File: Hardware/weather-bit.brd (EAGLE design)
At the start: 68.6 x 58.4 mm, 47 parts, among them J2 RJ11, J3 RJ11, J6 455-1750-1-ND, J7 455-1750-1-ND, J8 Qwiic (vertical), J9 1X04_SMD_STRAIGHT_COMBO, U1 BME280, U2 micro:bit

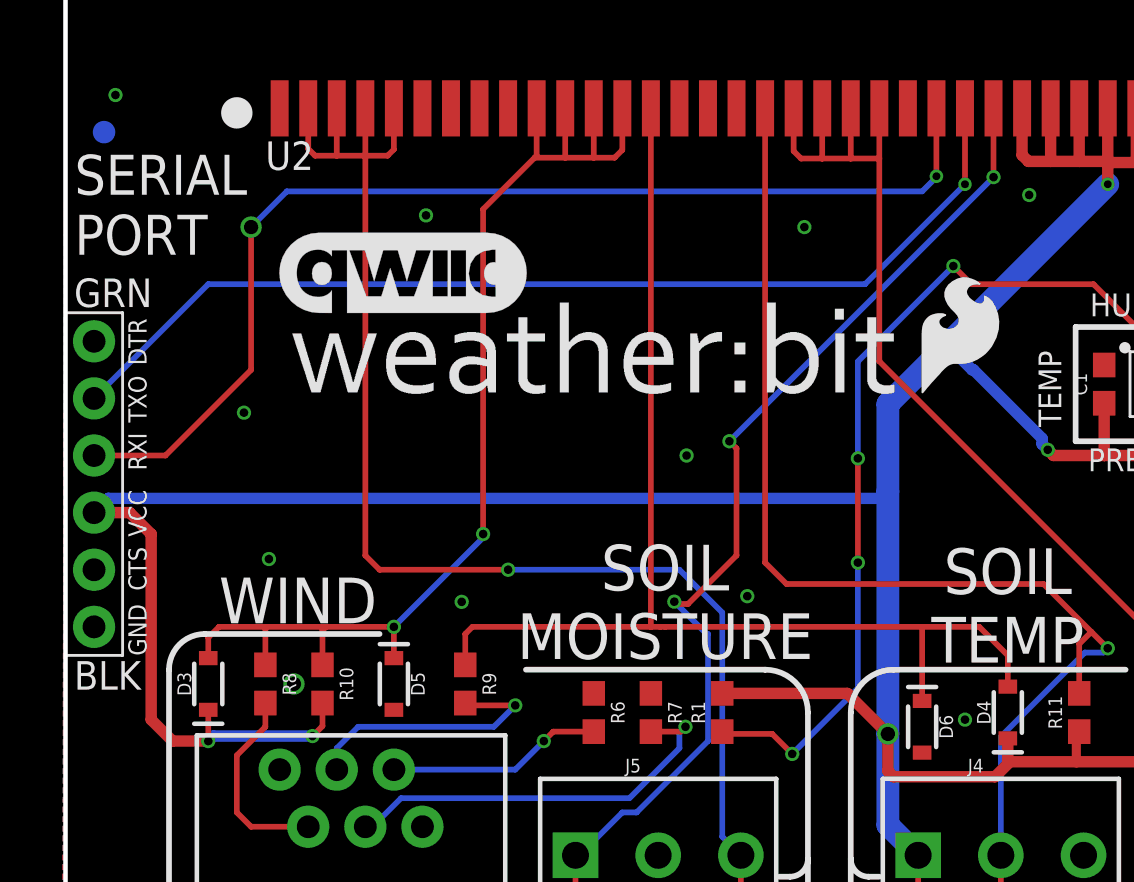
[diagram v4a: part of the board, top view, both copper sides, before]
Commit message: Moved to SMT vertical female header for Serial port
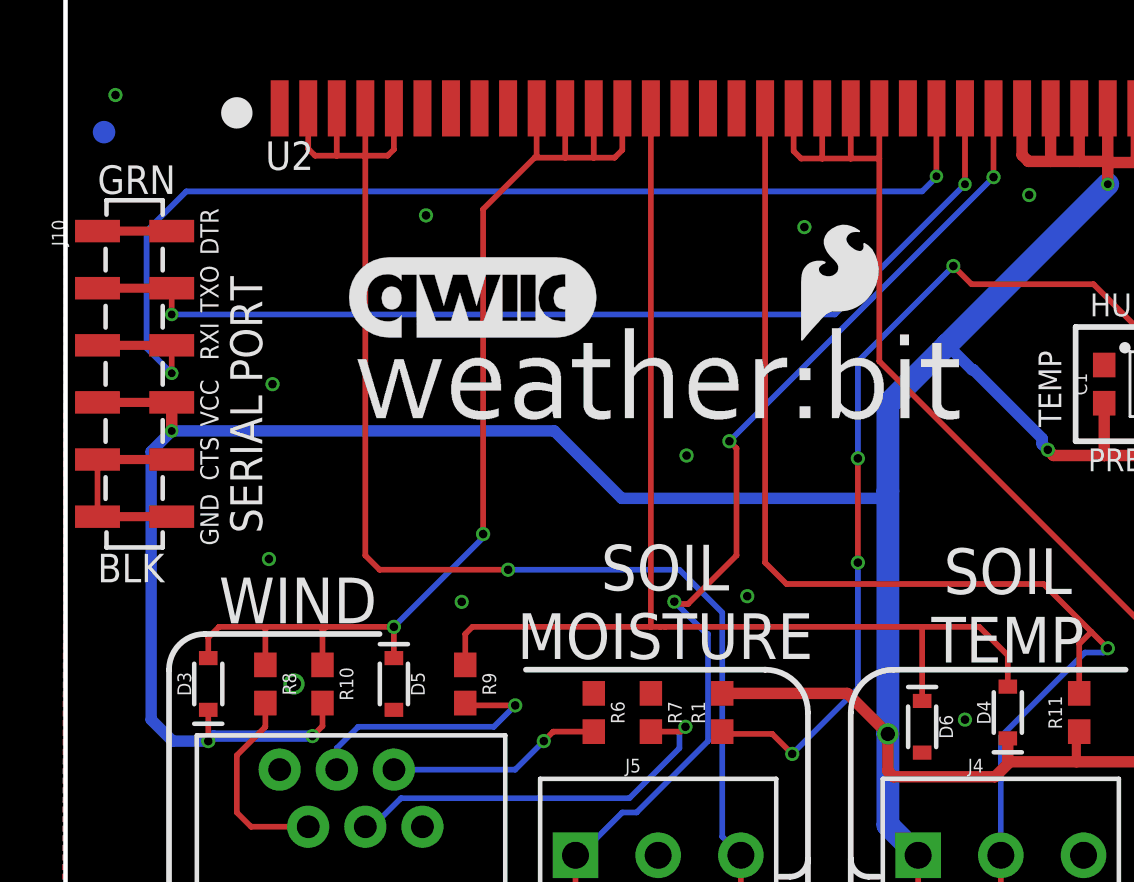
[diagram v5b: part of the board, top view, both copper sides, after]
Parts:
- removed J1: (no value), SparkFun-Connectors:6_PIN_SERIAL_TARGET_SIDE_W_SILK
- added J10: (no value), SparkFun-Connectors:6_PIN_SERIAL_TARGET_SIDE_VERT_SMT
- moved U$1 5.85 mm to (32.4, 35.3)
- moved U$6 3.29 mm to (18.1, 37.5)
- moved U$2 3.11 mm to (12.8, 31.9)
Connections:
- net 3.3V: now also J10.4, J10.4-2; no longer J1.P$4
- net GND: now also J10.5, J10.5-2, J10.6, J10.6-2; no longer J1.P$5, J1.P$6
- net RXI: now also J10.3, J10.3-2; no longer J1.P$3
- net TXO: now also J10.2, J10.2-2; no longer J1.P$2
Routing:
- net GND: track 0.00 -> 5.84 mm
- net 3.3V: track 191.9 -> 196.1 mm, vias 5 -> 6
- net RXI: track 49.4 -> 50.5 mm
- net TXO: track 46.1 -> 45.5 mm, vias 1 -> 2
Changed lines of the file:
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@@
 <text x="60.491371875" y="31.6103" size="0.8128" layer="21" font="vector" ratio="15" rot="SR0">SDA</text>
 <text x="60.54725" y="29.01441875" size="0.8128" layer="21" font="vector" ratio="15" rot="SR0">SCL</text>
-<text x="0.402765625" y="39.40965" size="1.778" layer="21" font="vector" ratio="15">SERIAL
-PORT</text>
+<text x="8.74875" y="27.021965625" size="1.4224" layer="21" font="vector" ratio="15" rot="R90">SERIAL PORT</text>
 <text x="62.007828125" y="39.382675" size="1.778" layer="21" font="vector" ratio="15">I2C
 PORT</text>
@@
 <attribute name="VALUE" value="1X04_SMD_STRAIGHT_COMBO" x="67.5132" y="28.2194" size="0.6096" layer="27" font="vector" ratio="20" rot="R90"/>
 </element>
-<element name="J1" library="SparkFun-Connectors" package="6_PIN_SERIAL_TARGET_SIDE_W_SILK" value="" x="1.27" y="29.21" smashed="yes" rot="R270"/>
-<element name="U$1" library="SparkFun-Aesthetics" package="SFE_LOGO_FLAME_.2" value="" x="37.762409375" y="33.012659375" smashed="yes"/>
-<element name="U$2" library="Micro_Bit_LOGOS" package="LOGO-WEATHERBIT" value="" x="9.907446875" y="33.02" smashed="yes"/>
+<element name="U$1" library="SparkFun-Aesthetics" package="SFE_LOGO_FLAME_.2" value="" x="32.403009375" y="35.349459375" smashed="yes"/>
+<element name="U$2" library="Micro_Bit_LOGOS" package="LOGO-WEATHERBIT" value="" x="12.803046875" y="31.877" smashed="yes"/>
 <element name="U$3" library="Micro_Bit_LOGOS" package="LOGO-WEATHERBIT" value="" x="42.4434" y="25.222196875" smashed="yes" rot="MR0"/>
 <element name="U$4" library="SparkFun-Aesthetics" package="ORDERING_INSTRUCTIONS" value="" x="1.143" y="-16.637" smashed="yes"/>
@@
 </element>
 <element name="U$5" library="SparkFun-Aesthetics" package="QWIIC_5MM" value="" x="57.4294" y="37.084" smashed="yes"/>
-<element name="U$6" library="SparkFun-Aesthetics" package="QWIIC_11MM" value="" x="15.0368" y="38.5572" smashed="yes"/>
+<element name="U$6" library="SparkFun-Aesthetics" package="QWIIC_11MM" value="" x="18.1356" y="37.465" smashed="yes"/>
 <element name="U$7" library="SparkFun-Aesthetics" package="QWIIC_11MM" value="" x="48.768" y="26.6954" smashed="yes" rot="MR0"/>
 <element name="U2" library="SparkFun-Connectors" package="MICRO:BIT-RA_SMD" value="micro:bit" x="34.29" y="52.07" smashed="yes">
@@
 <attribute name="VALUE" x="53.34" y="43.18" size="1.27" layer="27" font="vector"/>
 </element>
+<element name="J10" library="SparkFun-Connectors" package="6_PIN_SERIAL_TARGET_SIDE_VERT_SMT" value="" x="3.0734" y="40.4622" smashed="yes" rot="R270">
+<attribute name="NAME" x="-0.6096" y="40.9702" size="0.6096" layer="25" font="vector" ratio="20" rot="R270"/>
+<attribute name="VALUE" x="-1.4986" y="40.9702" size="0.6096" layer="27" font="vector" ratio="20" rot="R270"/>
+</element>
 </elements>
 <signals>
@@
 <polygon width="0.254" layer="1" isolate="0.3048">
 <vertex x="0" y="58.42"/>
-<vertex x="-0.13788125" y="-0.3175"/>
 <vertex x="-0.13788125" y="-0.3175"/>
 <vertex x="68.44211875" y="-0.3175"/>
@@
 <via x="65.56375" y="12.54125" extent="1-16" drill="0.381"/>
 <via x="66.04" y="45.4025" extent="1-16" drill="0.381"/>
-<via x="7.9375" y="32.385" extent="1-16" drill="0.381"/>
+<via x="9.2075" y="33.655" extent="1-16" drill="0.381"/>
 <via x="9.04875" y="25.87625" extent="1-16" drill="0.381"/>
 <via x="2.2225" y="46.51375" extent="1-16" drill="0.381"/>
@@
 <via x="10.16" y="20.32" extent="1-16" drill="0.635"/>
 <via x="13.97" y="10.16" extent="1-16" drill="0.381"/>
-<contactref element="J1" pad="P$6"/>
-<contactref element="J1" pad="P$5"/>
 <via x="60.48375" y="40.64" extent="1-16" drill="0.381"/>
 <via x="42.861228125" y="42.067478125" extent="1-16" drill="0.381"/>
@@
 <contactref element="U2" pad="P$35"/>
 <contactref element="U2" pad="P$36"/>
+<contactref element="J10" pad="5-2"/>
+<contactref element="J10" pad="5"/>
+<contactref element="J10" pad="6-2"/>
+<contactref element="J10" pad="6"/>
+<wire x1="4.7234" y1="30.3022" x2="1.4234" y2="30.3022" width="0.254" layer="1"/>
+<wire x1="1.4234" y1="30.3022" x2="1.4234" y2="27.7622" width="0.254" layer="1"/>
 </signal>
 <signal name="3.3V">
@@
 <wire x1="37.9222" y1="5.2578" x2="39.37" y2="3.81" width="0.254" layer="1"/>
 <contactref element="J9" pad="3"/>
-<contactref element="J1" pad="P$4"/>
 <via x="6.35" y="17.78" extent="1-16" drill="0.381"/>
 <via x="10.9855" y="18.00225" extent="1-16" drill="0.381"/>
@@
 <wire x1="36.83" y1="16.1925" x2="41.3385" y2="16.1925" width="0.508" layer="1"/>
 <wire x1="41.3385" y1="16.1925" x2="41.91" y2="16.764" width="0.508" layer="1"/>
-<wire x1="36.2585" y1="28.575" x2="36.576" y2="28.8925" width="0.508" layer="16"/>
-<wire x1="36.2585" y1="28.575" x2="1.905" y2="28.575" width="0.508" layer="16"/>
-<wire x1="1.27" y1="27.94" x2="2.8575" y2="27.94" width="0.508" layer="1"/>
-<wire x1="2.8575" y1="27.94" x2="3.81" y2="26.9875" width="0.508" layer="1"/>
-<wire x1="3.81" y1="26.9875" x2="3.81" y2="18.7325" width="0.508" layer="1"/>
-<wire x1="3.81" y1="18.7325" x2="4.7625" y2="17.78" width="0.508" layer="1"/>
-<wire x1="4.7625" y1="17.78" x2="6.35" y2="17.78" width="0.508" layer="1"/>
+<wire x1="36.576" y1="28.8925" x2="36.2585" y2="28.575" width="0.508" layer="16"/>
+<wire x1="4.7625" y1="17.78" x2="3.81" y2="18.7325" width="0.508" layer="16"/>
+<wire x1="4.7625" y1="17.78" x2="6.35" y2="17.78" width="0.508" layer="16"/>
 <wire x1="42.00525" y1="16.85925" x2="44.958" y2="16.85925" width="0.508" layer="1"/>
 <wire x1="44.958" y1="16.85925" x2="50.51425" y2="16.85925" width="0.508" layer="1"/>
@@
 <wire x1="41.91" y1="17.9" x2="41.91" y2="16.9545" width="0.508" layer="1"/>
 <wire x1="41.91" y1="16.9545" x2="42.00525" y2="16.85925" width="0.508" layer="1"/>
-<wire x1="1.905" y1="28.575" x2="1.27" y2="27.94" width="0.508" layer="16"/>
 <contactref element="R11" pad="1"/>
 <wire x1="43.434" y1="31.242" x2="43.434" y2="30.988" width="0.508" layer="16"/>
@@
 <wire x1="47.76125" y1="32.63" x2="47.76125" y2="30.49615" width="0.254" layer="1"/>
 <wire x1="47.76125" y1="30.49615" x2="47.7774" y2="30.48" width="0.254" layer="1"/>
+<contactref element="J10" pad="4"/>
+<contactref element="J10" pad="4-2"/>
+<wire x1="3.81" y1="30.6578" x2="4.7244" y2="31.5722" width="0.508" layer="16"/>
+<via x="4.7244" y="31.5722" extent="1-16" drill="0.35"/>
+<wire x1="3.81" y1="18.7325" x2="3.81" y2="30.6578" width="0.508" layer="16"/>
+<wire x1="4.7234" y1="32.8422" x2="4.7244" y2="32.8412" width="0.508" layer="1"/>
+<wire x1="4.7244" y1="32.8412" x2="4.7244" y2="31.5722" width="0.508" layer="1"/>
+<wire x1="21.7424" y1="31.5722" x2="4.7244" y2="31.5722" width="0.508" layer="16"/>
+<wire x1="36.2585" y1="28.575" x2="24.7396" y2="28.575" width="0.508" layer="16"/>
+<wire x1="24.7396" y1="28.575" x2="21.7424" y2="31.5722" width="0.508" layer="16"/>
+<wire x1="4.7234" y1="32.8422" x2="1.4234" y2="32.8422" width="0.254" layer="1"/>
 </signal>
 <signal name="N$2">
@@
 </signal>
 <signal name="RXI">
-<wire x1="9.8425" y1="42.2275" x2="38.1" y2="42.2275" width="0.254" layer="16"/>
-<contactref element="J1" pad="P$3"/>
-<via x="8.255" y="40.64" extent="1-16" drill="0.635"/>
-<wire x1="8.255" y1="34.29" x2="4.445" y2="30.48" width="0.254" layer="1"/>
-<wire x1="4.445" y1="30.48" x2="1.27" y2="30.48" width="0.254" layer="1"/>
-<wire x1="9.8425" y1="42.2275" x2="8.255" y2="40.64" width="0.254" layer="16"/>
-<wire x1="8.255" y1="34.29" x2="8.255" y2="40.64" width="0.254" layer="1"/>
 <contactref element="U2" pad="P$24"/>
-<wire x1="38.1" y1="42.2275" x2="38.735" y2="42.8625" width="0.254" layer="16"/>
+<wire x1="38.735" y1="42.8625" x2="38.1" y2="42.2275" width="0.254" layer="16"/>
 <wire x1="38.735" y1="42.8625" x2="38.735" y2="42.9006" width="0.254" layer="16"/>
 <via x="38.735" y="42.9006" extent="1-16" drill="0.35"/>
 <wire x1="38.735" y1="42.9006" x2="38.735" y2="45.92" width="0.254" layer="1"/>
+<contactref element="J10" pad="3-2"/>
+<contactref element="J10" pad="3"/>
+<wire x1="5.3721" y1="42.2275" x2="3.6068" y2="40.4622" width="0.254" layer="16"/>
+<wire x1="3.6068" y1="35.2552" x2="3.6068" y2="40.4622" width="0.254" layer="16"/>
+<wire x1="3.6068" y1="35.2552" x2="4.7244" y2="34.1376" width="0.254" layer="16"/>
+<via x="4.7244" y="34.1376" extent="1-16" drill="0.35"/>
+<wire x1="38.1" y1="42.2275" x2="5.3721" y2="42.2275" width="0.254" layer="16"/>
+<wire x1="4.7234" y1="35.3822" x2="1.4234" y2="35.3822" width="0.254" layer="1"/>
+<wire x1="4.7234" y1="35.3822" x2="4.7244" y2="35.3812" width="0.254" layer="1"/>
+<wire x1="4.7244" y1="35.3812" x2="4.7244" y2="34.1376" width="0.254" layer="1"/>
 </signal>
 <signal name="TXO">
-<wire x1="40.005" y1="42.545" x2="35.56" y2="38.1" width="0.254" layer="16"/>
-<wire x1="35.56" y1="38.1" x2="6.35" y2="38.1" width="0.254" layer="16"/>
-<contactref element="J1" pad="P$2"/>
-<wire x1="6.35" y1="38.1" x2="1.27" y2="33.02" width="0.254" layer="16"/>
 <contactref element="U2" pad="P$25"/>
 <wire x1="40.005" y1="45.92" x2="40.005" y2="42.545" width="0.254" layer="1"/>
 <via x="40.005" y="42.545" extent="1-16" drill="0.35"/>
+<contactref element="J10" pad="2-2"/>
+<contactref element="J10" pad="2"/>
+<wire x1="34.2138" y1="36.7538" x2="4.7244" y2="36.7538" width="0.254" layer="16"/>
+<via x="4.7244" y="36.7538" extent="1-16" drill="0.35"/>
+<wire x1="40.005" y1="42.545" x2="34.2138" y2="36.7538" width="0.254" layer="16"/>
+<wire x1="4.7244" y1="37.9212" x2="4.7244" y2="36.7538" width="0.254" layer="1"/>
+<wire x1="1.4234" y1="37.9222" x2="4.7234" y2="37.9222" width="0.254" layer="1"/>
+<wire x1="4.7234" y1="37.9222" x2="4.7244" y2="37.9212" width="0.254" layer="1"/>
 </signal>
 <signal name="11">

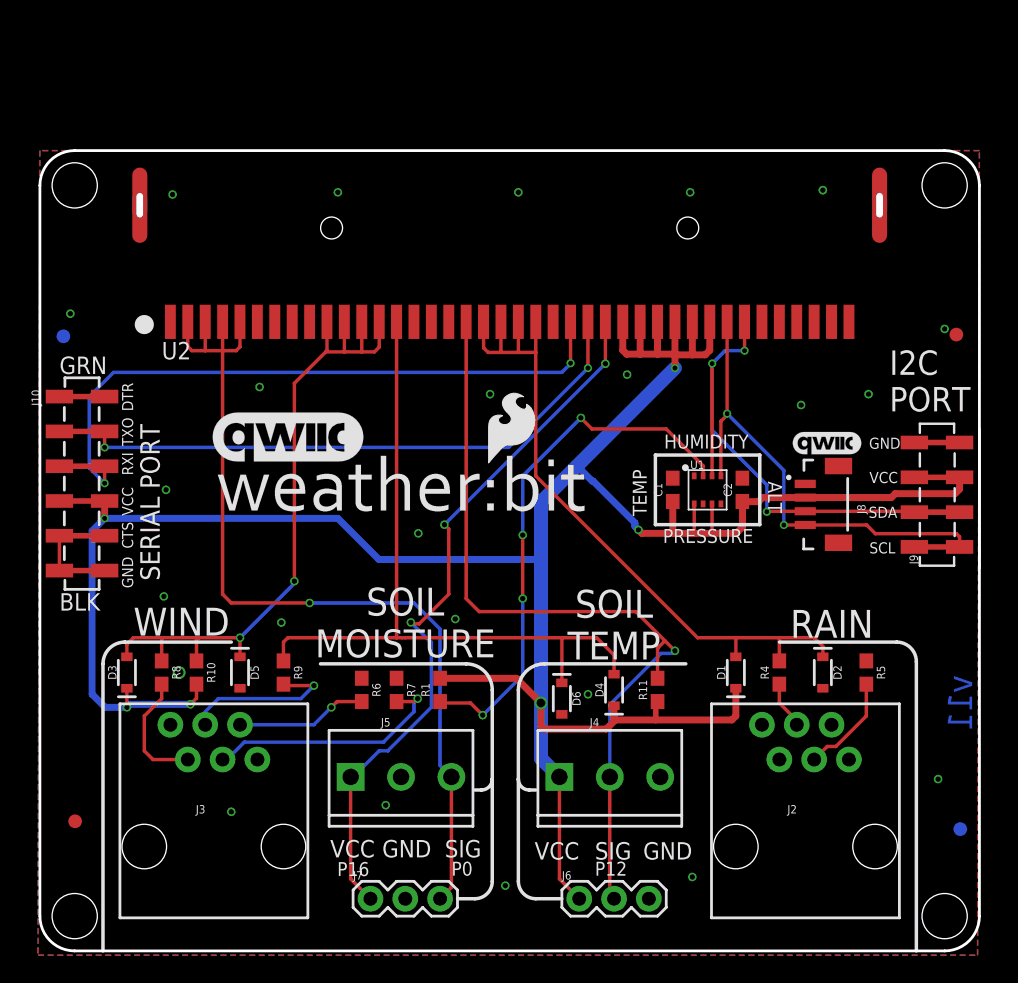
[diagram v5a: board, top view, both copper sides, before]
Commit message: SMT serial header and buzzard silk update
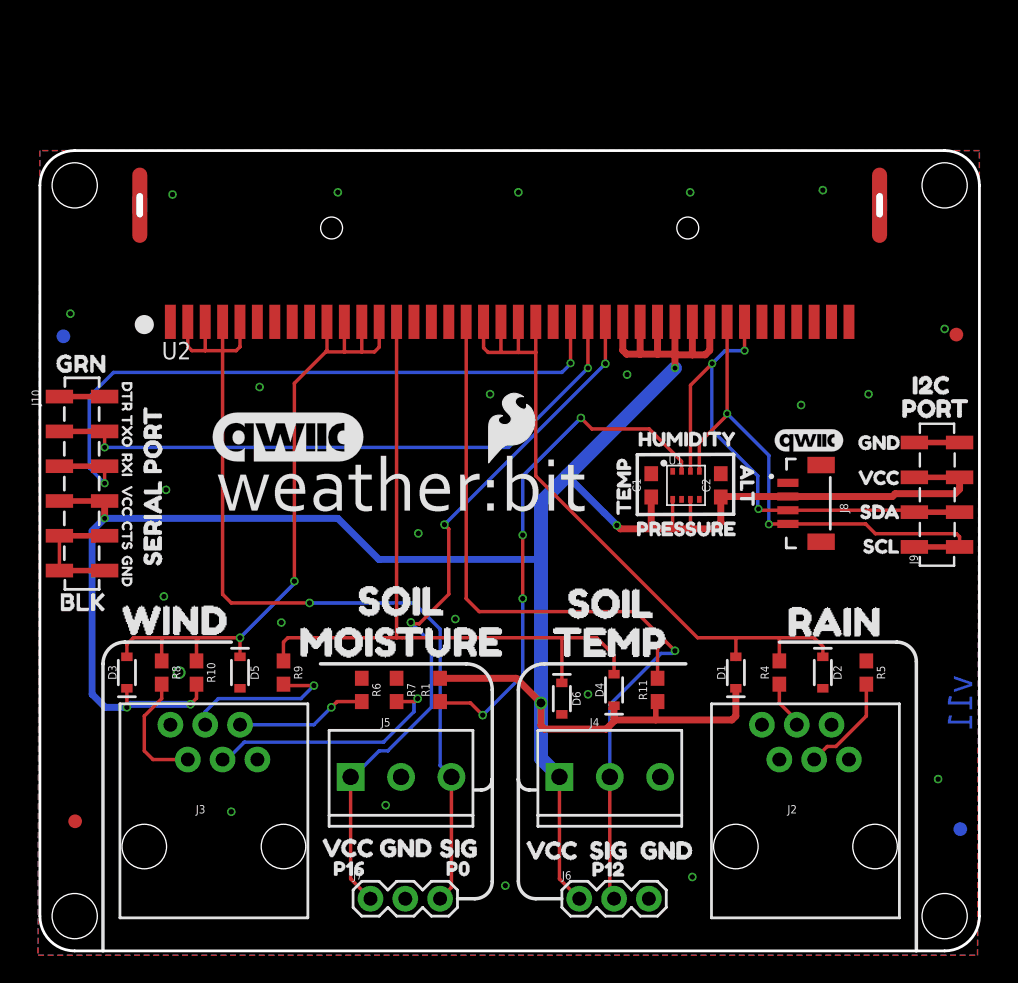
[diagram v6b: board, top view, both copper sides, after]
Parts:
- added U$10: (no value), buzzard_labels:SERIAL_PORT0
- added U$11: (no value), buzzard_labels:WIND12
- added U$12, U$13: (no value), buzzard_labels:SOIL13
- added U$14: (no value), buzzard_labels:MOISTURE14
- added U$15: (no value), buzzard_labels:TEMP15
- added U$16: (no value), buzzard_labels:RAIN16
- added U$17, U$21: (no value), buzzard_labels:VCC6
- added U$18, U$22: (no value), buzzard_labels:GND7
- added U$19, U$20: (no value), buzzard_labels:SIG8
- added U$23: (no value), buzzard_labels:P169
- added U$24: (no value), buzzard_labels:P010
- added U$25: (no value), buzzard_labels:P1211
- added U$26: (no value), buzzard_labels:HUMIDITY3
- added U$27: (no value), buzzard_labels:TEMP4
- added U$28: (no value), buzzard_labels:PRESSURE5
- added U$29: (no value), buzzard_labels:GND18
- added U$30: (no value), buzzard_labels:VCC19
- added U$31: (no value), buzzard_labels:SDA20
- added U$32: (no value), buzzard_labels:SCL21
- added U$33: (no value), buzzard_labels:SPARKFUN#COM#MICROBIT17
- added U$34: (no value), buzzard_labels (1):ALT0
- added U$8: (no value), buzzard_labels:I2C1
- added U$9: (no value), buzzard_labels:PORT2
- J10: value (none) -> SMD
- J9: value 1X04_SMD_STRAIGHT_COMBO -> SMD
- moved C1 1.61 mm to (44.6, 34.0)
- moved C2 1.61 mm to (49.7, 34.0)
- moved U1 1.61 mm to (47.2, 34.0)
- moved U$5 1.34 mm to (56.1, 37.3)
- moved J8 1.27 mm to (53.8, 32.7)
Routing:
- net N$2: track 39.4 -> 37.6 mm
- net SCL: track 35.2 -> 36.2 mm
- net SDA: track 36.4 -> 36.9 mm
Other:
- board text removed: "ALT"
- board text removed: "GND"
- board text removed: "HUMIDITY"
- board text removed: "I2C PORT"
- board text removed: "P0"
- board text removed: "P12"
- board text removed: "P16"
- board text removed: "PRESSURE"
- board text removed: "RAIN"
- board text removed: "SCL"
- board text removed: "SDA"
- board text removed: "SERIAL PORT"
- board text removed: "SIG"
- board text removed: "SOIL MOISTURE"
- board text removed: "SOIL TEMP"
- board text removed: "TEMP"
- board text removed: "VCC"
- board text removed: "WIND"
- board text removed: "sparkfun.com/microbit"
